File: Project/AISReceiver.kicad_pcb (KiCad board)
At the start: 2 copper layers, 48 x 78.2 mm, 73 parts, among them J1 SPI, J2 CONN_01X20, J3 CONN_01X20, J5 CONN_01X01, Q1 2.5A/30V, Q2 MBT3904DW1, U1 ESP32-WROOM, U2 AP2112K-3.3V, U3 MCP73811T-420I/OT, U4 LIS331HH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

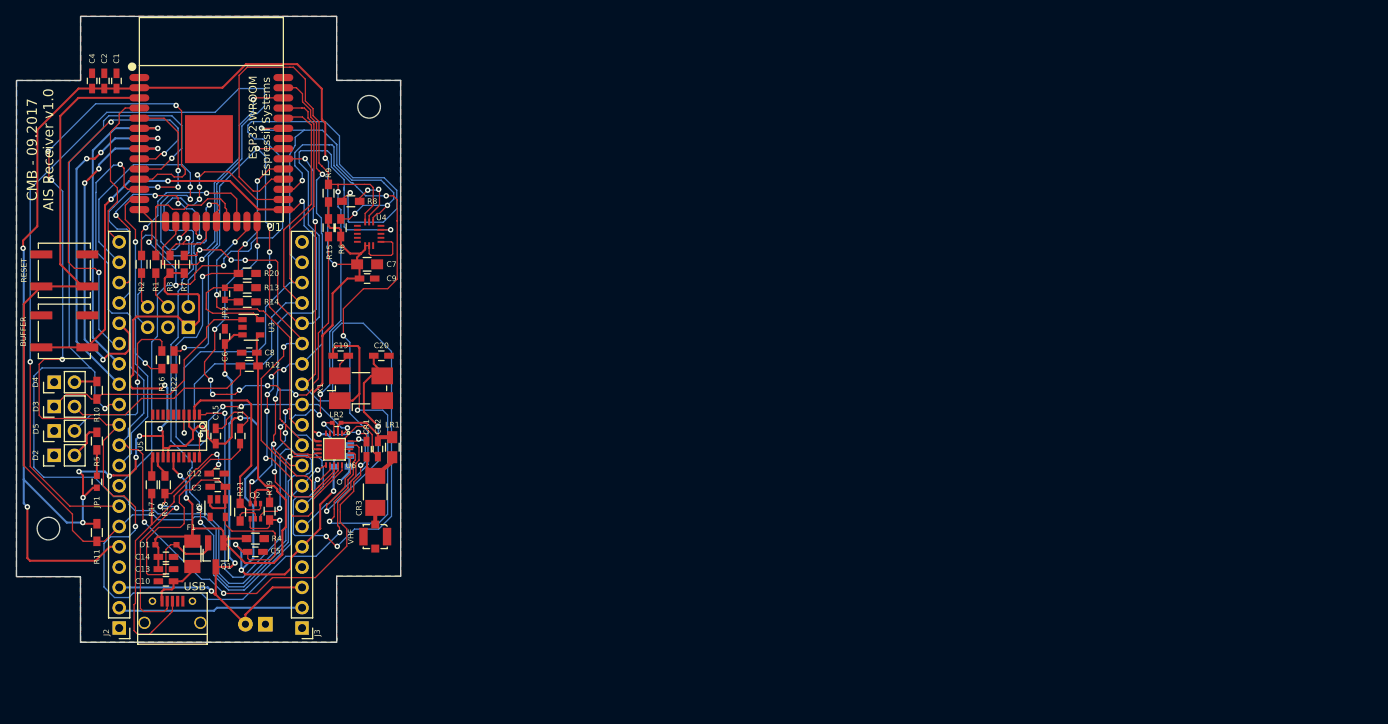
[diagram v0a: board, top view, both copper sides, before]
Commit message: AIS specific board.
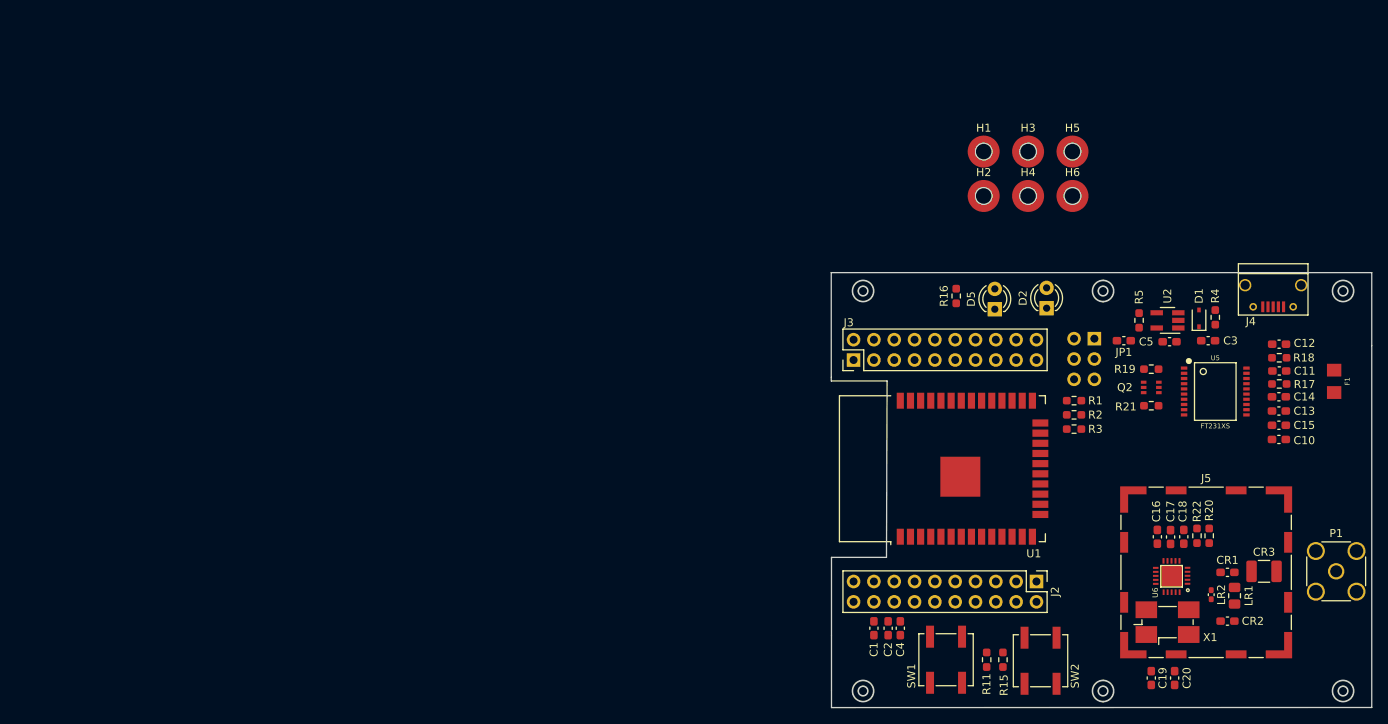
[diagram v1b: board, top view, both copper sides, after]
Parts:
- removed BATT: JP2, Connectors_JST:JST_EH_S02B-EH_02x2.50mm_Angled
- removed BUFFER: BUFFER_RESET, Buttons_Switches_SMD:SW_SPST_B3SL-1002P
- removed C6, C8: 4.7uF, Capacitors_SMD:C_0603_HandSoldering
- removed C7: 10uF, Capacitors_SMD:C_0805_HandSoldering
- removed C9: 0.1uF, Capacitors_SMD:C_0603_HandSoldering
- removed D3: RED, Pin_Headers:Pin_Header_Straight_1x02_Pitch2.54mm
- removed D4: BLUE, Pin_Headers:Pin_Header_Straight_1x02_Pitch2.54mm
- removed JP2: Jumper, Capacitors_SMD:C_0603
- removed Q1: 2.5A/30V, TO_SOT_Packages_SMD:SOT-23_Handsoldering
- removed R10, R12: 1K, Resistors_SMD:R_0603_HandSoldering
- removed R13, R14: 2K, Resistors_SMD:R_0603_HandSoldering
- removed R6, R7: 4.7K, Resistors_SMD:R_0603_HandSoldering
- removed R8: 100R, Resistors_SMD:R_0603_HandSoldering
- removed R9: 10K, Resistors_SMD:R_0603_HandSoldering
- removed RESET: RESET, Buttons_Switches_SMD:SW_SPST_B3SL-1002P
- removed U3: MCP73811T-420I/OT, TO_SOT_Packages_SMD:SOT-23-5
- removed U4: LIS331HH, Si4464:LGA-16-3x3
- removed USB: USB_OTG, Si4464:USB_Micro-B
- removed VHF: Antenna, Connectors_Molex:Molex_Microcoaxial_RF
- added H1: MountingHole_Pad, Mounting_Wuerth:Mounting_Wuerth_WA-SMSI-M1.6_H1.5mm_9774015633, F.Cu at (144.0, 37.7)
- added H2: MountingHole_Pad, Mounting_Wuerth:Mounting_Wuerth_WA-SMSI-M1.6_H1.5mm_9774015633, F.Cu at (144.0, 43.3)
- added H3: MountingHole_Pad, Mounting_Wuerth:Mounting_Wuerth_WA-SMSI-M1.6_H1.5mm_9774015633, F.Cu at (149.6, 37.7)
- added H4: MountingHole_Pad, Mounting_Wuerth:Mounting_Wuerth_WA-SMSI-M1.6_H1.5mm_9774015633, F.Cu at (149.6, 43.3)
- added H5: MountingHole_Pad, Mounting_Wuerth:Mounting_Wuerth_WA-SMSI-M1.6_H1.5mm_9774015633, F.Cu at (155.1, 37.7)
- added H6: MountingHole_Pad, Mounting_Wuerth:Mounting_Wuerth_WA-SMSI-M1.6_H1.5mm_9774015633, F.Cu at (155.1, 43.3)
- added J4: USB_OTG, Si4464:USB_Micro-B, F.Cu at (180.2, 55.8)
- added J5: RF_Shield, RF_Shielding:Wuerth_36103205_20x20mm, F.Cu at (171.8, 90.3)
- added P1: Antenna, Connector_Coaxial:SMA_Amphenol_132134_Vertical, F.Cu at (188.1, 90.2)
- added SW1: RESET, Button_Switch_SMD:SW_SPST_B3SL-1022P, F.Cu at (139.3, 101.2)
- added SW2: BUFFER_RESET, Button_Switch_SMD:SW_SPST_B3SL-1022P, F.Cu at (151.1, 101.3)
- C1, C10, C11, C12, C13, C14, C15, C19, C2, C20, C3, C4, C5, CR1, CR2: footprint Capacitors_SMD:C_0603_HandSoldering -> Capacitor_SMD:C_0603_1608Metric_Pad1.08x0.95mm_HandSolder
- C16, C17, C18: footprint Capacitors_SMD:C_0603_HandSoldering -> Capacitor_SMD:C_0603_1608Metric_Pad1.08x0.95mm_HandSolder; moved to F.Cu
- CR3: footprint Capacitors_SMD:C_1210_HandSoldering -> Capacitor_SMD:C_1210_3225Metric_Pad1.33x2.70mm_HandSolder
- D1: footprint Si4464:SOD-323 -> Diode_SMD:D_SOD-323
- D2, D5: footprint Pin_Headers:Pin_Header_Straight_1x02_Pitch2.54mm -> LED_THT:LED_D3.0mm_Clear
- F1: footprint Fuse_Holders_and_Fuses:Fuse_SMD1206_Wave -> Fuses:1206
- J2, J3: footprint Pin_Headers:Pin_Header_Straight_1x20_Pitch2.54mm -> Connector_PinHeader_2.54mm:PinHeader_2x10_P2.54mm_Vertical
- JP1: footprint Capacitors_SMD:C_0603 -> Capacitor_SMD:C_0603_1608Metric_Pad1.08x0.95mm_HandSolder
- LR1: footprint Capacitors_SMD:C_0805_HandSoldering -> Capacitor_SMD:C_0805_2012Metric_Pad1.18x1.45mm_HandSolder
- LR2: footprint Capacitors_SMD:C_0402 -> Capacitor_SMD:C_0402_1005Metric_Pad0.74x0.62mm_HandSolder
- R1, R11, R15, R16, R17, R18, R19, R2, R20, R21, R22, R3, R4, R5: footprint Resistors_SMD:R_0603_HandSoldering -> Resistor_SMD:R_0603_1608Metric_Pad0.98x0.95mm_HandSolder
- U1: footprint ESP32-footprints-Lib:ESP32-WROOM -> RF_Module:ESP32-WROOM-32
- U2: footprint TO_SOT_Packages_SMD:SOT-23-5 -> Package_TO_SOT_SMD:SOT-23-5_HandSoldering
- U5: footprint SMD_Packages:SSOP-20 -> Silicon-Standard:SSOP_20
- X1: footprint Crystals:Crystal_SMD_0603-4pin_6.0x3.5mm_HandSoldering -> Crystal:Crystal_SMD_0603-4Pin_6.0x3.5mm_HandSoldering
- moved F1 144.3 mm to (187.8, 66.4)
- moved R17 141.5 mm to (181.0, 66.8), turned to 180 degrees
- moved C14 140.6 mm to (180.9, 68.4)
- moved C13 140.5 mm to (180.9, 70.1)
- moved C10 140.2 mm to (180.9, 73.7), turned to 0 degrees
- moved R18 140.2 mm to (181.0, 63.5), turned to 180 degrees
- moved C12 133.8 mm to (180.9, 61.8)
- moved C15 132.9 mm to (180.9, 71.9), turned to 0 degrees
- moved D1 132.2 mm to (170.9, 58.5), turned to 90 degrees
- moved R5 131.1 mm to (163.4, 58.8)
- moved C11 130.1 mm to (181.0, 65.1), turned to 0 degrees
- moved U5 130.0 mm to (173.0, 67.7), turned to 0 degrees
- moved R22 129.7 mm to (170.7, 85.7)
- moved JP1 129.6 mm to (161.5, 61.3), turned to 180 degrees
- moved D2 125.4 mm to (151.9, 57.3)
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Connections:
- J2 pad 3: V_BATT -> Net-(J2-Pad3)
- J3 pad 3: V_BATT -> Net-(J3-Pad3)
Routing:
- net 3.3V: track 350.3 -> 0.00 mm, vias 17 -> 0
- net GPIO2: track 154.3 -> 0.00 mm, vias 6 -> 0
- net CHIP_PU: track 139.4 -> 0.00 mm, vias 1 -> 0
- net GPIO1: track 138.1 -> 0.00 mm, vias 3 -> 0
- net 0: track 125.9 -> 0.00 mm, vias 7 -> 0
- net 13: track 118.3 -> 0.00 mm, vias 2 -> 0
- net ACC_SDO: track 112.2 -> 0.00 mm, vias 4 -> 0
- net GPIO3: track 108.1 -> 0.00 mm, vias 5 -> 0
- net ACC_CS: track 104.2 -> 0.00 mm, vias 3 -> 0
- net SCLK: track 101.3 -> 0.00 mm, vias 5 -> 0
- net nIRQ: track 99.0 -> 0.00 mm, vias 6 -> 0
- net SCL: track 93.8 -> 0.00 mm, vias 5 -> 0
- net SDO: track 91.4 -> 0.00 mm, vias 6 -> 0
- net 16: track 74.7 -> 0.00 mm, vias 3 -> 0
- net SDN: track 70.7 -> 0.00 mm, vias 6 -> 0
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- removed copper zone on B.Cu, net GND
- removed copper zone on F.Cu, net GND
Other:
- board size 48 x 78.2 mm -> 67.6 x 54.4 mm
- board text removed: "3.3V"
- board text removed: "CLK"
- board text removed: "CMB - 09.2017 AIS Receiver v1.0"
- board text removed: "CS"
- board text removed: "GND"
- board text removed: "MISO"
- board text removed: "MOSI"

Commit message: Initial tracing.
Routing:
- net 0: track 0.00 -> 59.6 mm
- net 3.3V: track 0.00 -> 33.1 mm
- net CHIP_PU: track 0.00 -> 32.4 mm
- net V_USB: track 0.00 -> 28.7 mm
- net USB-RAW: track 0.00 -> 14.7 mm
- net SDO: track 0.00 -> 13.5 mm
- net Net-(C20-Pad1): track 0.00 -> 11.6 mm
- net SDN: track 0.00 -> 10.7 mm, vias 0 -> 2
- net Net-(C11-Pad1): track 0.00 -> 10.6 mm
- net VIN: track 0.00 -> 8.70 mm
- net Net-(CR3-Pad1): track 0.00 -> 7.45 mm
- net Net-(C12-Pad1): track 0.00 -> 6.70 mm
- net Net-(CR1-Pad2): track 0.00 -> 6.42 mm
- net DTR: track 0.00 -> 5.83 mm
- net Net-(CR2-Pad2): track 0.00 -> 5.32 mm
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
